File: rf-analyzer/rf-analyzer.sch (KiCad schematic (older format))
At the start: 75 parts, among them U1 AD8302, U2 AD8302, U3 OPA695

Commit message: Removed LMX2322 from schematic.
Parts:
- removed C?: 100nF, Capacitor_SMD:C_0603_1608Metric_Pad1.05x0.95mm_HandSolder, symbol Device:C_Small
- removed C?: 100pF, Capacitor_SMD:C_0603_1608Metric_Pad1.05x0.95mm_HandSolder, symbol Device:C_Small
- removed C? (x2): 1nF, Capacitor_SMD:C_0603_1608Metric_Pad1.05x0.95mm_HandSolder, symbol Device:C_Small
- removed U?: LMX2322, symbol linear:LMX2322
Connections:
- net labels removed: CPo_count, LE_count, clk_count, data_count
- wire segments 333 -> 291
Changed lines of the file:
@@
 Text GLabel 6350 6150 2    50   Input ~ 0
 SCL
-$Comp
-L linear:LMX2322 U?
-U 1 1 5CBB56B2
-P 5750 4050
-F 0 "U?" H 5900 4400 50  0000 C CNN
-F 1 "LMX2322" H 5500 4400 50  0000 C CNN
-F 2 "" H 5750 4050 50  0001 C CNN
-F 3 "" H 5750 4050 50  0001 C CNN
-	1    5750 4050
-	1    0    0    -1
-$EndComp
-$Comp
-L Device:C_Small C?
-U 1 1 5CBE660B
-P 5900 3450
-F 0 "C?" V 6000 3400 50  0000 L CNN
-F 1 "100nF" V 5800 3350 50  0000 L CNN
-F 2 "Capacitor_SMD:C_0603_1608Metric_Pad1.05x0.95mm_HandSolder" H 5900 3450 50  0001 C CNN
-F 3 "" H 5900 3450 50  0001 C CNN
-	1    5900 3450
-	0    1    1    0
-$EndComp
-$Comp
-L Device:C_Small C?
-U 1 1 5CBE6611
-P 5900 3150
-F 0 "C?" V 6000 3100 50  0000 L CNN
-F 1 "100pF" V 5800 3050 50  0000 L CNN
-F 2 "Capacitor_SMD:C_0603_1608Metric_Pad1.05x0.95mm_HandSolder" H 5900 3150 50  0001 C CNN
-F 3 "" H 5900 3150 50  0001 C CNN
-	1    5900 3150
-	0    1    1    0
-$EndComp
-Wire Wire Line
-	5800 3150 5750 3150
-Wire Wire Line
-	5750 3450 5800 3450
-Wire Wire Line
-	6000 3150 6050 3150
-Wire Wire Line
-	6050 3150 6050 3450
-Wire Wire Line
-	6000 3450 6050 3450
-Wire Wire Line
-	6200 3450 6200 3500
-Connection ~ 6050 3450
-Wire Wire Line
-	5750 3100 5750 3150
-Connection ~ 5750 3150
-Connection ~ 5750 3450
-Wire Wire Line
-	6050 3450 6200 3450
-Wire Wire Line
-	5750 3150 5750 3450
-Wire Wire Line
-	5750 3450 5750 3600
-$Comp
-L power:GNDA #PWR?
-U 1 1 5CBE6624
-P 6200 3500
-F 0 "#PWR?" H 6200 3250 50  0001 C CNN
-F 1 "GNDA" H 6205 3327 50  0000 C CNN
-F 2 "" H 6200 3500 50  0001 C CNN
-F 3 "" H 6200 3500 50  0001 C CNN
-	1    6200 3500
-	1    0    0    -1
-$EndComp
-$Comp
-L power:+5V #PWR?
-U 1 1 5CBE662A
-P 5750 3100
-F 0 "#PWR?" H 5750 2950 50  0001 C CNN
-F 1 "+5V" H 5765 3273 50  0000 C CNN
-F 2 "" H 5750 3100 50  0001 C CNN
-F 3 "" H 5750 3100 50  0001 C CNN
-	1    5750 3100
-	1    0    0    -1
-$EndComp
-Wire Wire Line
-	5400 3900 5300 3900
-Wire Wire Line
-	5300 3900 5300 3600
-Wire Wire Line
-	5300 3600 5750 3600
-Connection ~ 5750 3600
-Wire Wire Line
-	5750 3600 5750 3650
-Wire Wire Line
-	6100 3850 6100 3600
-Wire Wire Line
-	6100 3600 5750 3600
-$Comp
-L Device:C_Small C?
-U 1 1 5CC34D51
-P 6350 4050
-F 0 "C?" V 6250 4100 50  0000 L CNN
-F 1 "1nF" V 6250 3900 50  0000 L CNN
-F 2 "Capacitor_SMD:C_0603_1608Metric_Pad1.05x0.95mm_HandSolder" H 6350 4050 50  0001 C CNN
-F 3 "" H 6350 4050 50  0001 C CNN
-	1    6350 4050
-	0    1    1    0
-$EndComp
-$Comp
-L Device:C_Small C?
-U 1 1 5CC3546D
-P 6200 4450
-F 0 "C?" V 6100 4500 50  0000 L CNN
-F 1 "1nF" V 6100 4300 50  0000 L CNN
-F 2 "Capacitor_SMD:C_0603_1608Metric_Pad1.05x0.95mm_HandSolder" H 6200 4450 50  0001 C CNN
-F 3 "" H 6200 4450 50  0001 C CNN
-	1    6200 4450
-	1    0    0    1
-$EndComp
-Wire Wire Line
-	6100 4150 6200 4150
-Wire Wire Line
-	6200 4150 6200 4050
-Wire Wire Line
-	6200 4050 6250 4050
-$Comp
-L power:GNDA #PWR?
-U 1 1 5CDED4F4
-P 5750 4500
-F 0 "#PWR?" H 5750 4250 50  0001 C CNN
-F 1 "GNDA" H 5755 4327 50  0000 C CNN
-F 2 "" H 5750 4500 50  0001 C CNN
-F 3 "" H 5750 4500 50  0001 C CNN
-	1    5750 4500
-	1    0    0    -1
-$EndComp
-Wire Wire Line
-	5750 4450 5750 4500
-$Comp
-L power:GNDA #PWR?
-U 1 1 5CEB809E
-P 6200 4600
-F 0 "#PWR?" H 6200 4350 50  0001 C CNN
-F 1 "GNDA" H 6205 4427 50  0000 C CNN
-F 2 "" H 6200 4600 50  0001 C CNN
-F 3 "" H 6200 4600 50  0001 C CNN
-	1    6200 4600
-	1    0    0    -1
-$EndComp
 Text GLabel 10350 3800 2    50   Input ~ 0
 freq_count
@@
 	10250 3800 10350 3800
 Connection ~ 10250 3700
-Wire Wire Line
-	6100 4250 6200 4250
-Wire Wire Line
-	6200 4250 6200 4350
-Wire Wire Line
-	6200 4550 6200 4600
-Wire Wire Line
-	6550 4050 6450 4050
 $Comp
 L arduino:Arduino_Due_Shield XA?
@@
 Wire Wire Line
 	1100 4300 1050 4300
-Text GLabel 5250 4100 0    50   Input ~ 0
-data_count
-Text GLabel 5250 3950 0    50   Input ~ 0
-clk_count
-Text GLabel 5250 4250 0    50   Input ~ 0
-LE_count
-Text GLabel 6350 3800 2    50   Input ~ 0
-CPo_count
-Wire Wire Line
-	6100 3950 6150 3950
-Wire Wire Line
-	6150 3950 6150 3800
-Wire Wire Line
-	6150 3800 6350 3800
-Wire Wire Line
-	5400 4100 5250 4100
-Wire Wire Line
-	5400 4000 5350 4000
-Wire Wire Line
-	5350 4000 5350 3950
-Wire Wire Line
-	5350 3950 5250 3950
-Wire Wire Line
-	5400 4200 5350 4200
-Wire Wire Line
-	5350 4200 5350 4250
-Wire Wire Line
-	5350 4250 5250 4250
-Text GLabel 3950 3100 2    50   Input ~ 0
-CPo_count
-Text GLabel 3950 3250 2    50   Input ~ 0
-clk_count
-Text GLabel 3950 3400 2    50   Input ~ 0
-LE_count
-Text GLabel 1050 3250 0    50   Input ~ 0
-data_count
-Wire Wire Line
-	3800 3250 3950 3250
-Wire Wire Line
-	3800 3350 3850 3350
-Wire Wire Line
-	3850 3350 3850 3400
-Wire Wire Line
-	3850 3400 3950 3400
-Wire Wire Line
-	3800 3150 3850 3150
-Wire Wire Line
-	3850 3150 3850 3100
-Wire Wire Line
-	3850 3100 3950 3100
-Wire Wire Line
-	1200 3250 1050 3250
 Wire Notes Line
 	9550 5650 8750 5650

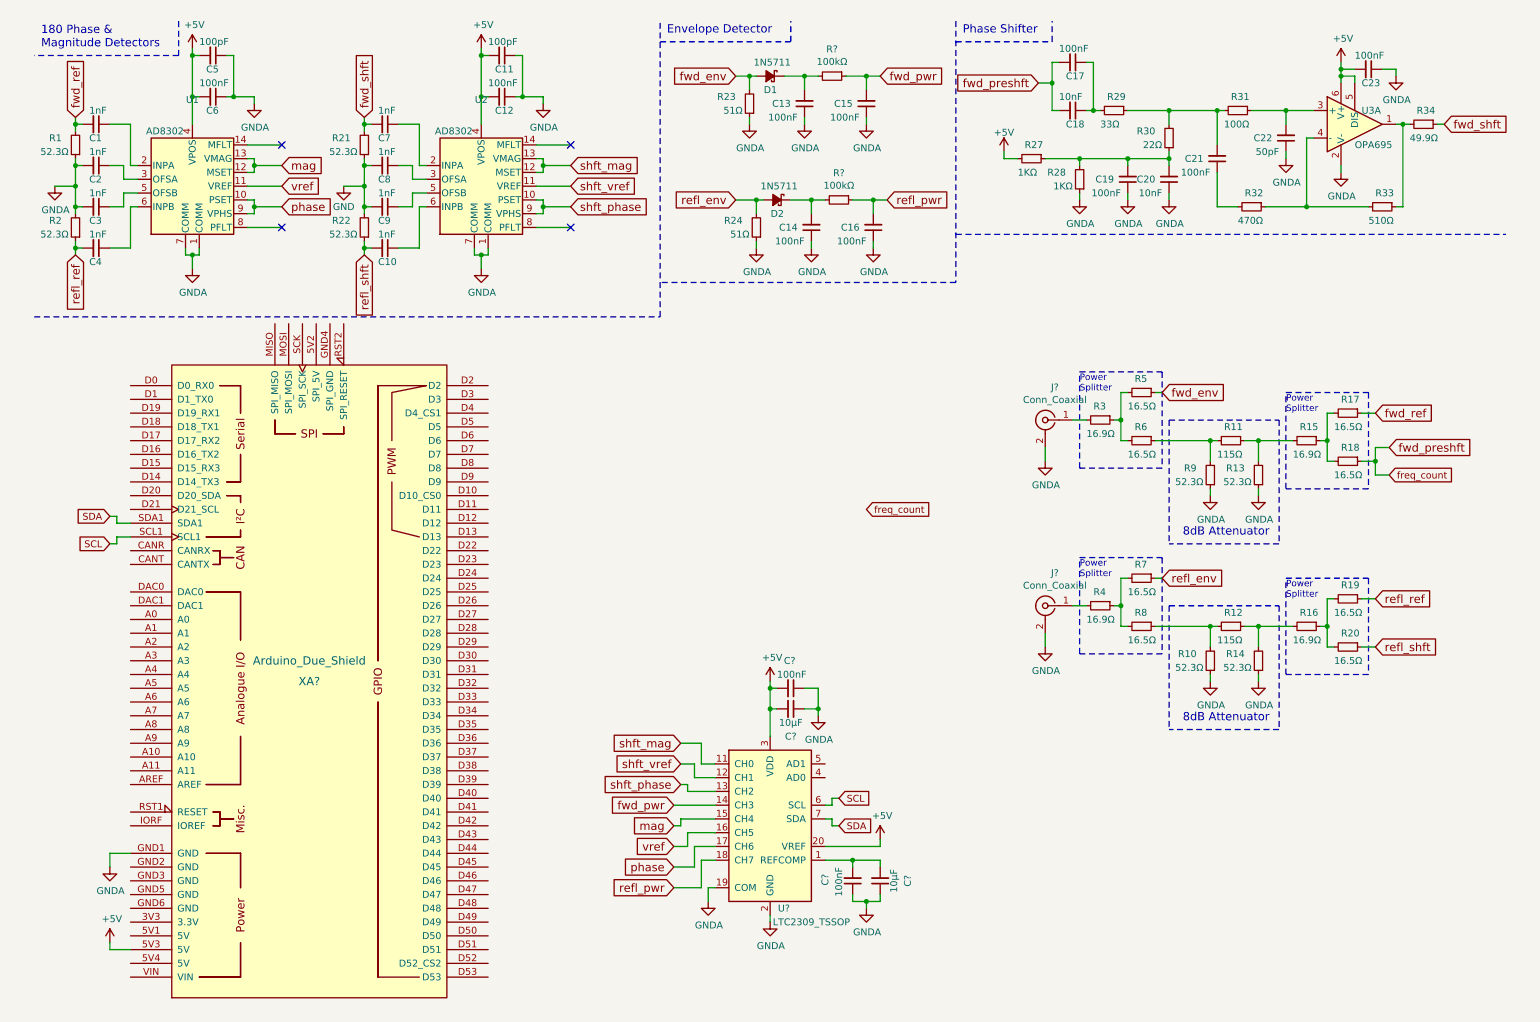
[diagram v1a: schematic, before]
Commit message: Updated power rails to be safer for the arduino Due.
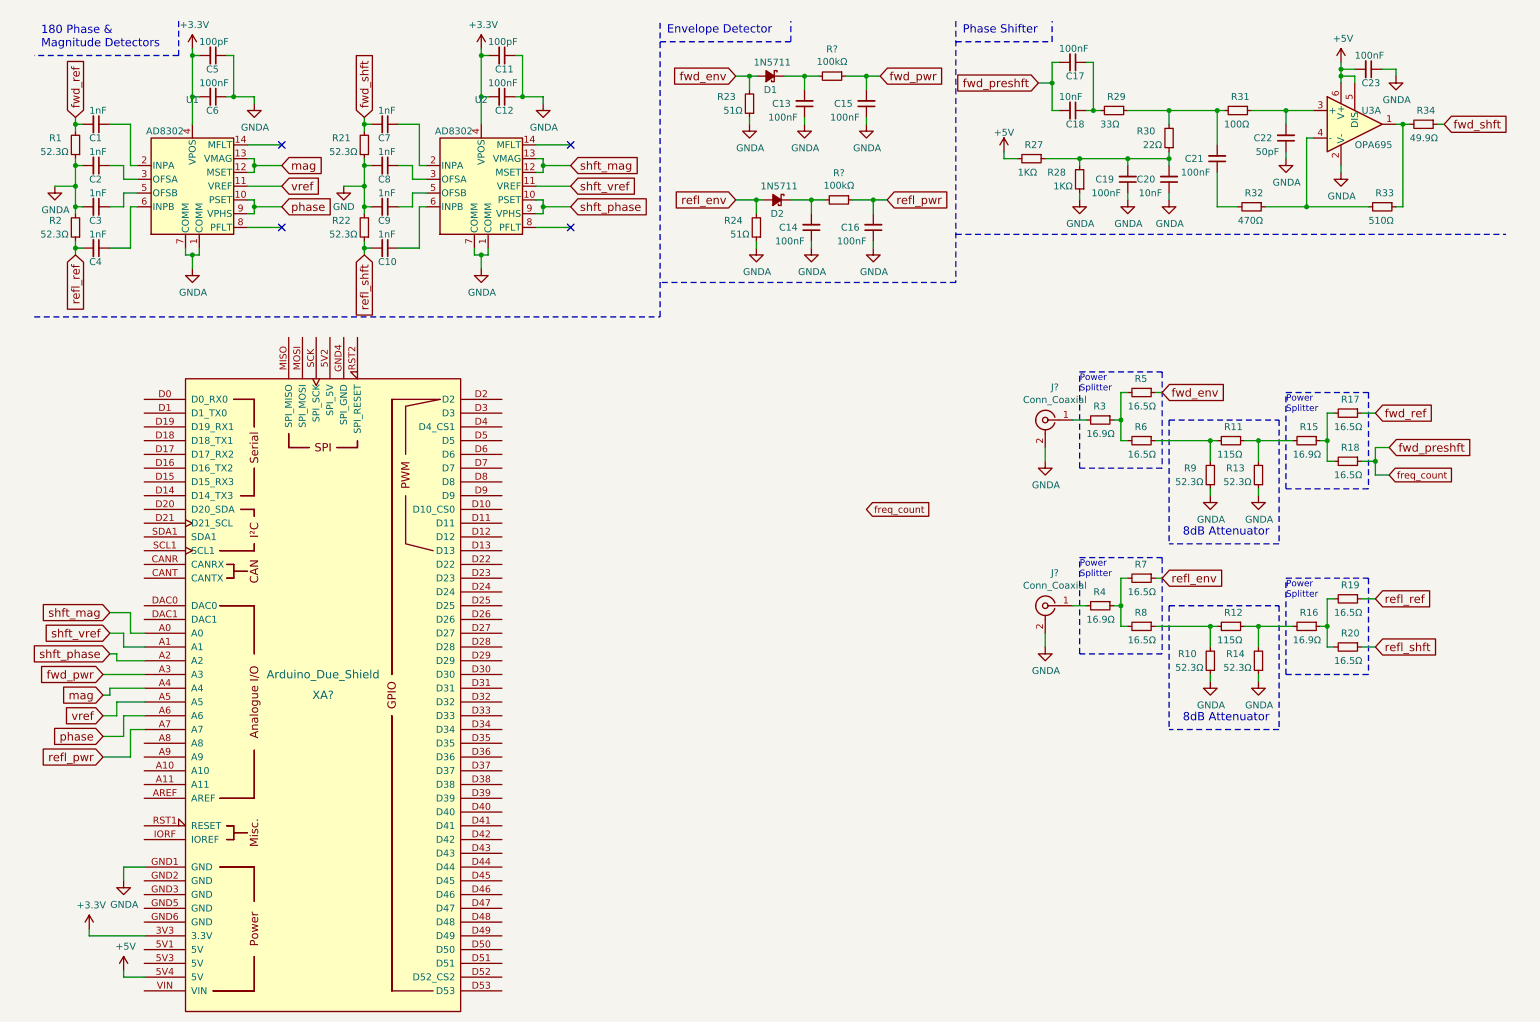
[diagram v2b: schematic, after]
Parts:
- removed C? (x2): 100nF, Capacitor_SMD:C_0603_1608Metric_Pad1.05x0.95mm_HandSolder, symbol Device:C_Small
- removed C? (x2): 10μF, symbol Device:C_Small
- removed U?: LTC2309_TSSOP, Package_SO:TSSOP-20_4.4x6.5mm_P0.65mm, symbol Analog_ADC:LTC2309_TSSOP
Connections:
- net +5V: now also XA?.5V4 (5V); no longer C11.2, C12.2, C5.2, C6.2, U1.4 (VPOS), U2.4 (VPOS), XA?.5V3 (5V)
- net fwd_pwr: now also XA?.A3
- net mag: now also XA?.A4
- net phase: now also XA?.A6
- net refl_pwr: now also XA?.A7
- net shft_mag: now also XA?.A0
- net shft_phase: now also XA?.A2
- net shft_vref: now also XA?.A1
- net vref: now also XA?.A5
- net +3V3: now reaches XA?.3V3 (3.3V)
- net +3V3: now also C11.2, C12.2, C5.2, C6.2, U1.4 (VPOS), U2.4 (VPOS)
- net SCL: no longer names the net of XA?.SCL1
- net SDA: no longer names the net of XA?.SDA1
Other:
- moved on the sheet: XA?

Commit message: Revert "Updated power rails to be safer for the arduino Due."
This reverts commit 4777d5e6577dfa59df44698bd1e5544e157ec2ab.
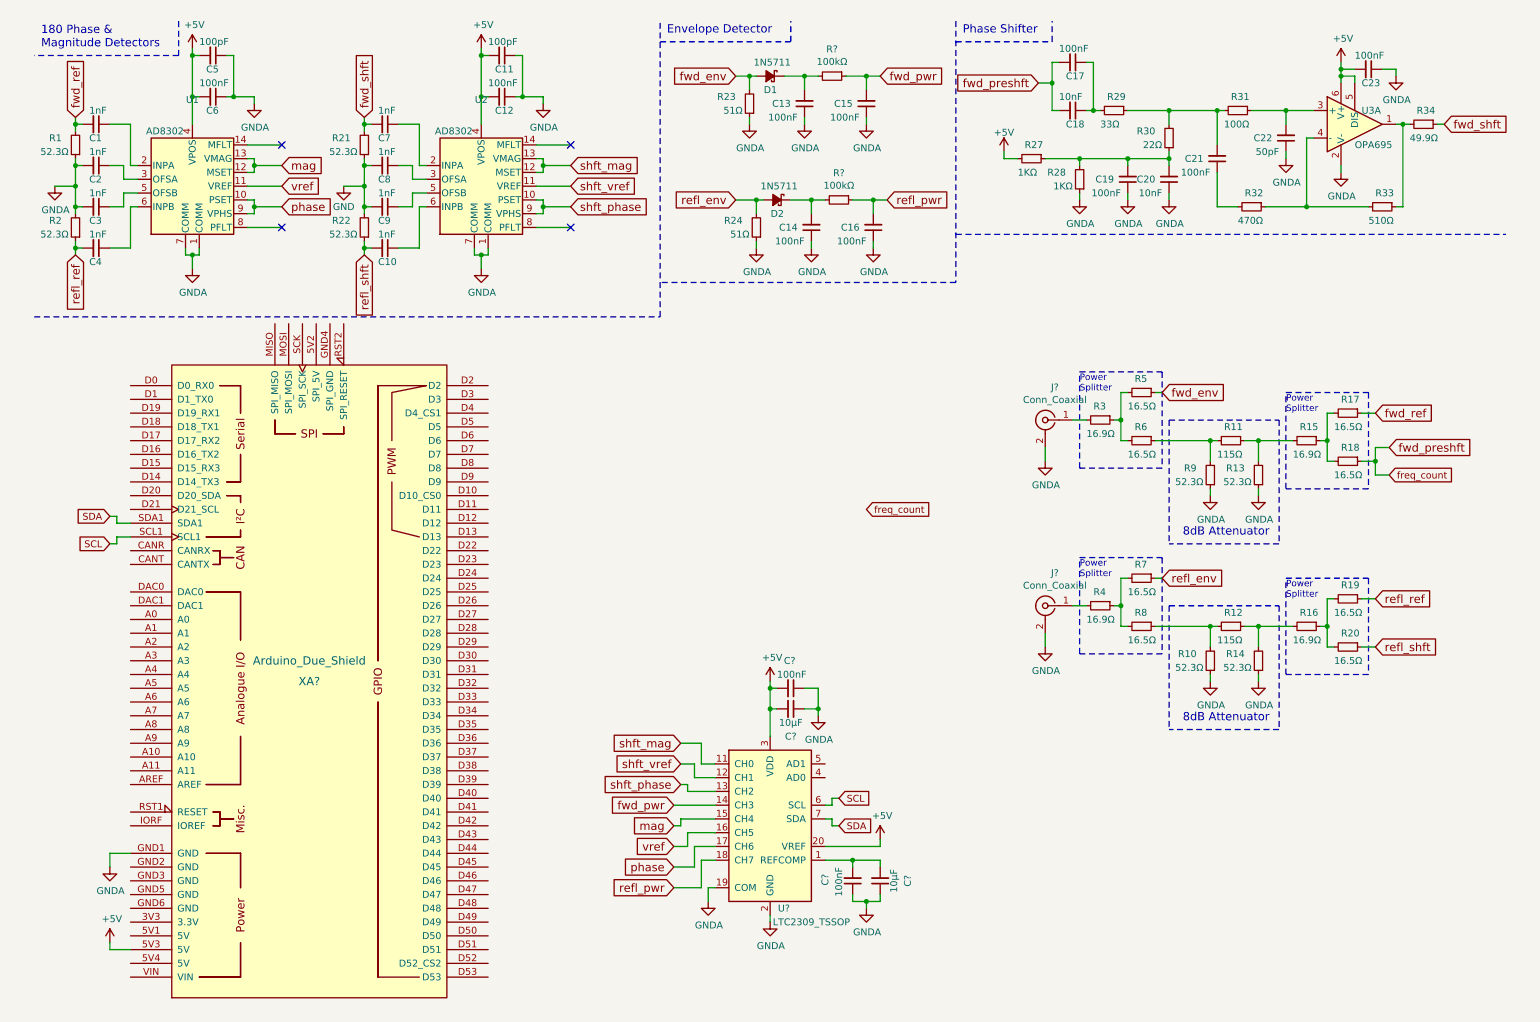
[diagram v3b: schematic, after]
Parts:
- added C? (x2): 100nF, Capacitor_SMD:C_0603_1608Metric_Pad1.05x0.95mm_HandSolder, symbol Device:C_Small
- added C? (x2): 10μF, symbol Device:C_Small
- added U?: LTC2309_TSSOP, Package_SO:TSSOP-20_4.4x6.5mm_P0.65mm, symbol Analog_ADC:LTC2309_TSSOP
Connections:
- net +5V: now also C11.2, C12.2, C5.2, C6.2, U1.4 (VPOS), U2.4 (VPOS), XA?.5V3 (5V), C?.2, C?.2, U?.10 (VDD), U?.20 (VREF), U?.3 (VDD); no longer XA?.5V4 (5V)
- net GNDA: now also C?.1, C?.1, C?.1, C?.1, U?.19 (COM), U?.2 (GND), U?.8 (GND), U?.9 (GND)
- net fwd_pwr: now also U?.14 (CH3); no longer XA?.A3
- net mag: now also U?.15 (CH4); no longer XA?.A4
- net phase: now also U?.17 (CH6); no longer XA?.A6
- net refl_pwr: now also U?.18 (CH7); no longer XA?.A7
- net shft_mag: now also U?.11 (CH0); no longer XA?.A0
- net shft_phase: now also U?.13 (CH2); no longer XA?.A2
- net shft_vref: now also U?.12 (CH1); no longer XA?.A1
- net vref: now also U?.16 (CH5); no longer XA?.A5
- net SCL: now reaches XA?.SCL1
- net SCL: now also U?.6 (SCL)
- net SDA: now reaches XA?.SDA1
- net SDA: now also U?.7 (SDA)
- removed net +3V3: C11.2, C12.2, C5.2, C6.2, U1.4 (VPOS), U2.4 (VPOS), XA?.3V3 (3.3V)
- new net: C?.2, C?.2, U?.1 (REFCOMP)
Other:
- moved on the sheet: XA?

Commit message: Eliminated power splitters and attenuator.
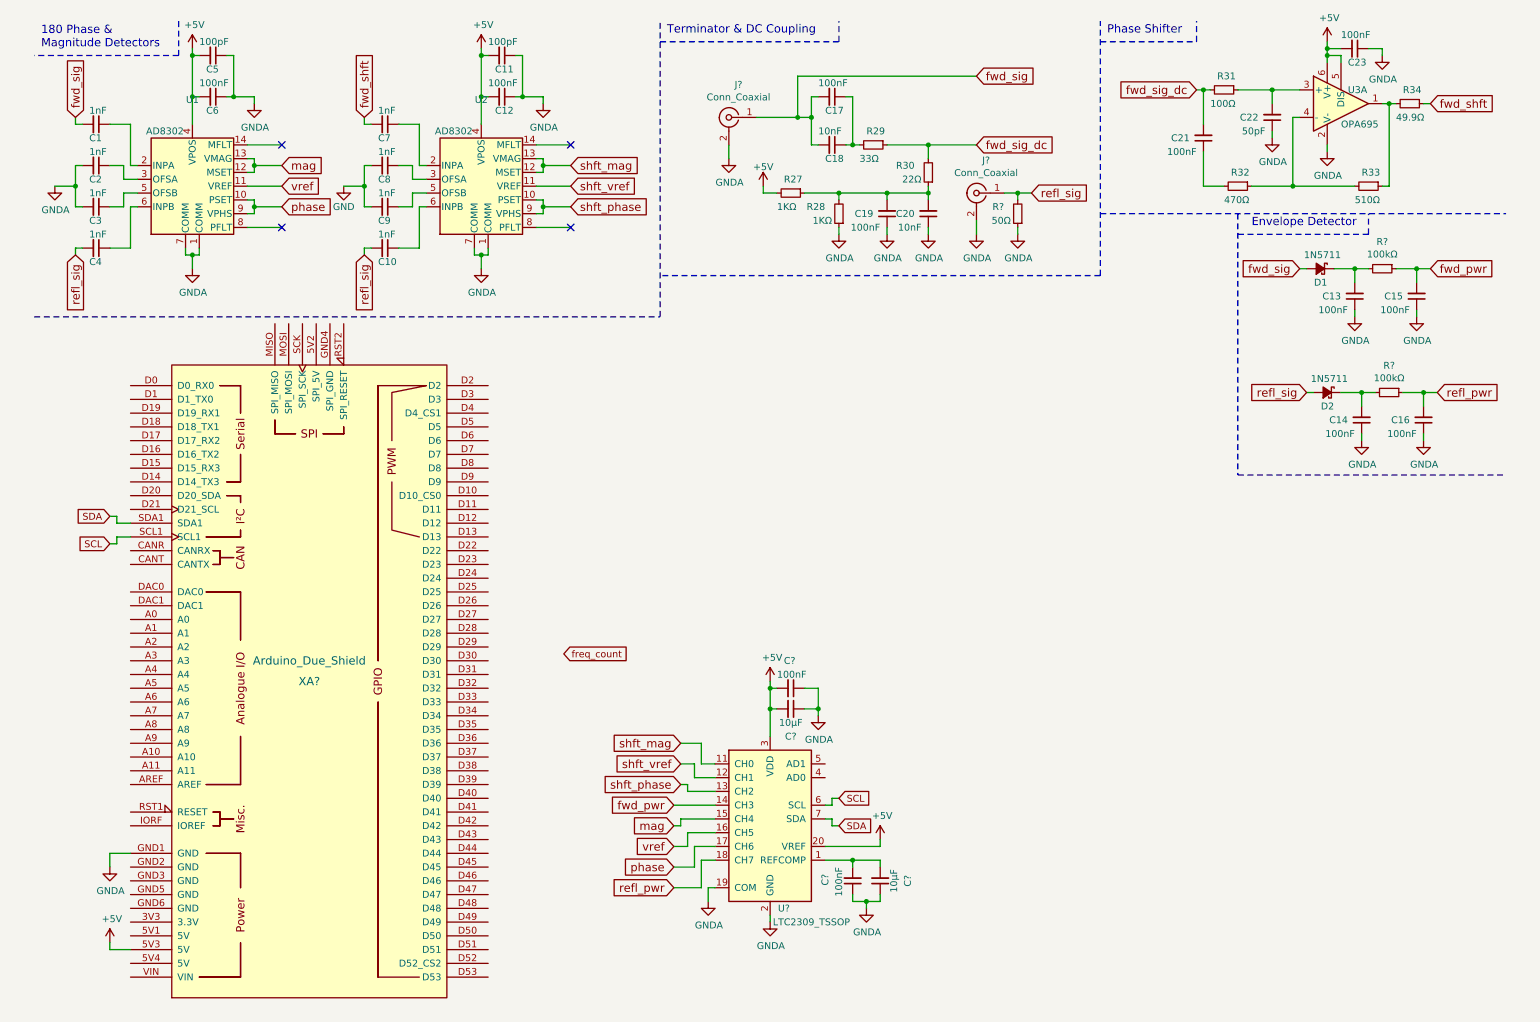
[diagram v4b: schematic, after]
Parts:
- removed R1, R2, R21, R22: 52.3Ω, Resistor_SMD:R_0603_1608Metric_Pad1.05x0.95mm_HandSolder, symbol Device:R_Small
- removed R10, R13, R14, R9: 52.3Ω, Resistor_SMD:R_1206_3216Metric_Pad1.42x1.75mm_HandSolder, symbol Device:R_Small
- removed R11, R12: 115Ω, Resistor_SMD:R_1206_3216Metric_Pad1.42x1.75mm_HandSolder, symbol Device:R_Small
- removed R15, R16: 16.9Ω, Resistor_SMD:R_0805_2012Metric_Pad1.15x1.40mm_HandSolder, symbol Device:R_Small
- removed R17, R18, R19, R20: 16.5Ω, Resistor_SMD:R_0805_2012Metric_Pad1.15x1.40mm_HandSolder, symbol Device:R_Small
- removed R23, R24: 51Ω, Resistor_SMD:R_0603_1608Metric_Pad1.05x0.95mm_HandSolder, symbol Device:R_Small
- removed R3, R4: 16.9Ω, Resistor_SMD:R_1206_3216Metric_Pad1.42x1.75mm_HandSolder, symbol Device:R_Small
- removed R5, R6, R7, R8: 16.5Ω, Resistor_SMD:R_1206_3216Metric_Pad1.42x1.75mm_HandSolder, symbol Device:R_Small
- added R?: 50Ω, Resistor_SMD:R_0603_1608Metric_Pad1.05x0.95mm_HandSolder, symbol Device:R_Small
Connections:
- net fwd_env is gone; now on net fwd_sig: D1.2 (A)
- net fwd_ref is gone; now on net fwd_sig: C1.2
- net refl_env is gone; now on net refl_sig: D2.2 (A)
- net refl_ref is gone; now on net refl_sig: C4.2
- net refl_shft is gone; now on net refl_sig: C10.2
- net GNDA: now also R?.1
- net freq_count: no longer C17.2, C18.2
- net fwd_sig_dc: now reaches C21.2, R29.1, R30.2, R31.2
- net fwd_sig: now reaches J?.1 (In)
- net fwd_sig: now also C17.2, C18.2
- net refl_sig: now reaches J?.1 (In)
- net refl_sig: now also R?.2
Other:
- note added: "Terminator & DC Coupling"
- note removed: "8dB Attenuator"
- note removed: "Power\nSplitter"
- moved on the sheet: C13, C14, C15, C16, C17, C18, C19, C20, C21, C22, C23, D1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

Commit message: Cleaned up the ADC.
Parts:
- added C?: 2.2μF, symbol Device:C_Small
- added R? (x2): 1.7KΩ, Resistor_SMD:R_0603_1608Metric_Pad1.05x0.95mm_HandSolder, symbol Device:R_Small
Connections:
- net +5V: no longer U?.20 (VREF)
- net GNDA: now also C?.1
- net SCL: now also R?.1
- net SDA: now also R?.1
- new net: C?.2, U?.20 (VREF)
- new net +3V3: R?.2, R?.2
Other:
- note added: "Analog-Digital Converter"
- moved on the sheet: C?, U?
